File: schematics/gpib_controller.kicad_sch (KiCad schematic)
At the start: 22 parts, among them SW1 SW_DIP_x06, U1 74LS366, U10 74LS04, U12 2716, U2 74LS138

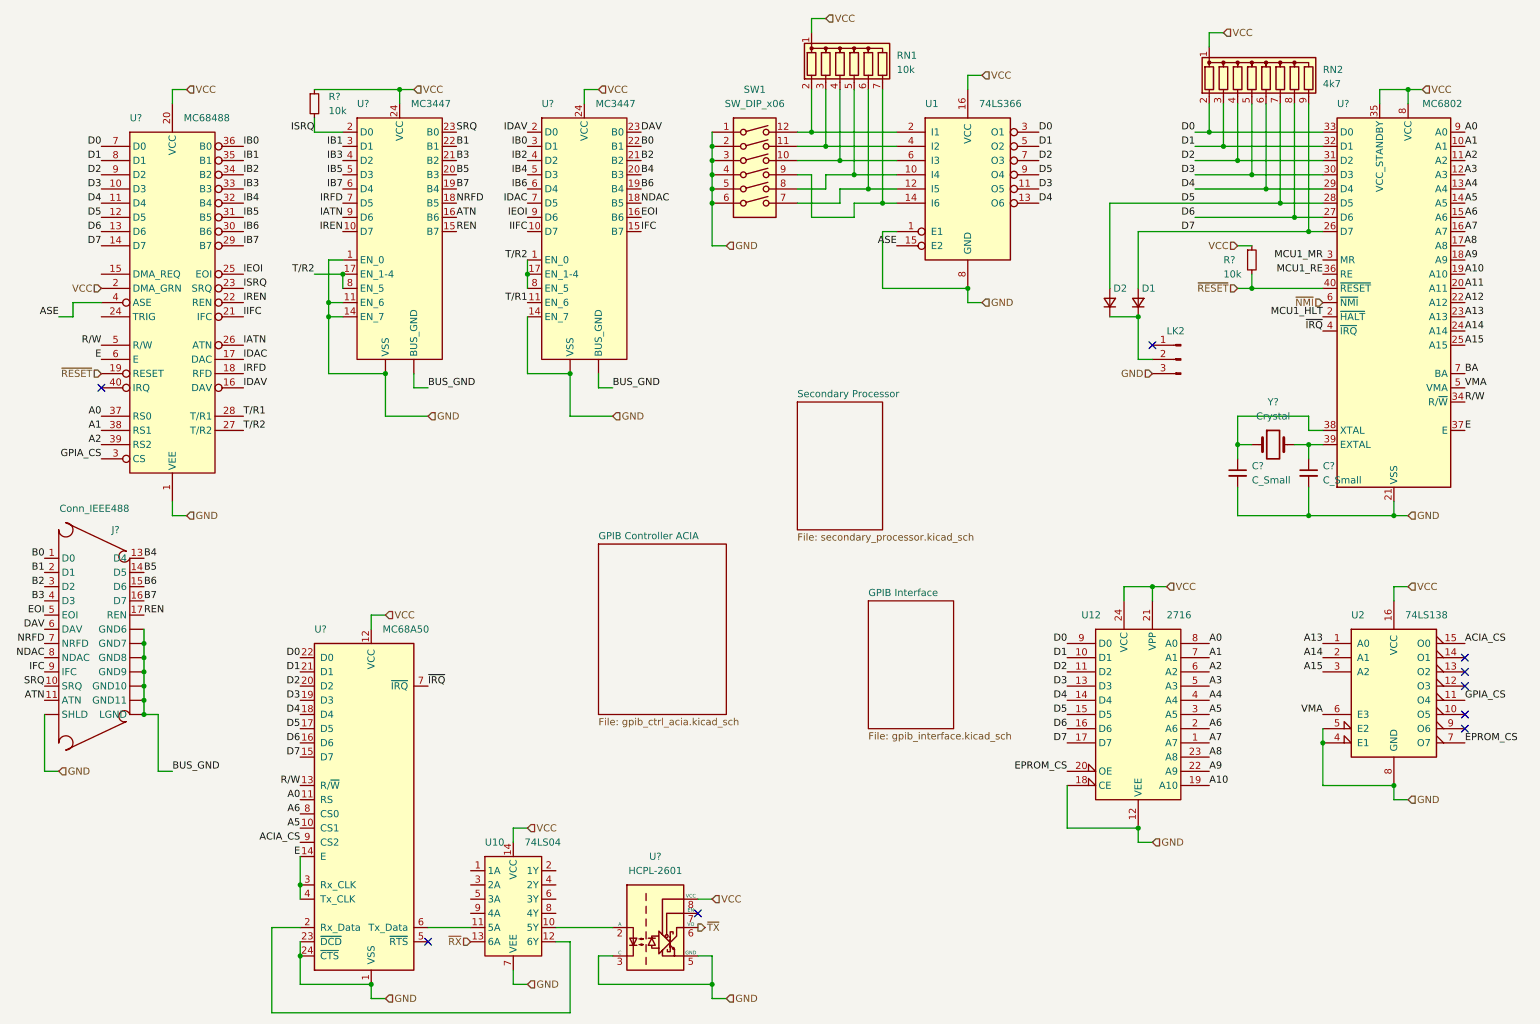
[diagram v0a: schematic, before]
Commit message: Moved more components into hierachical sheets, misc cleanup
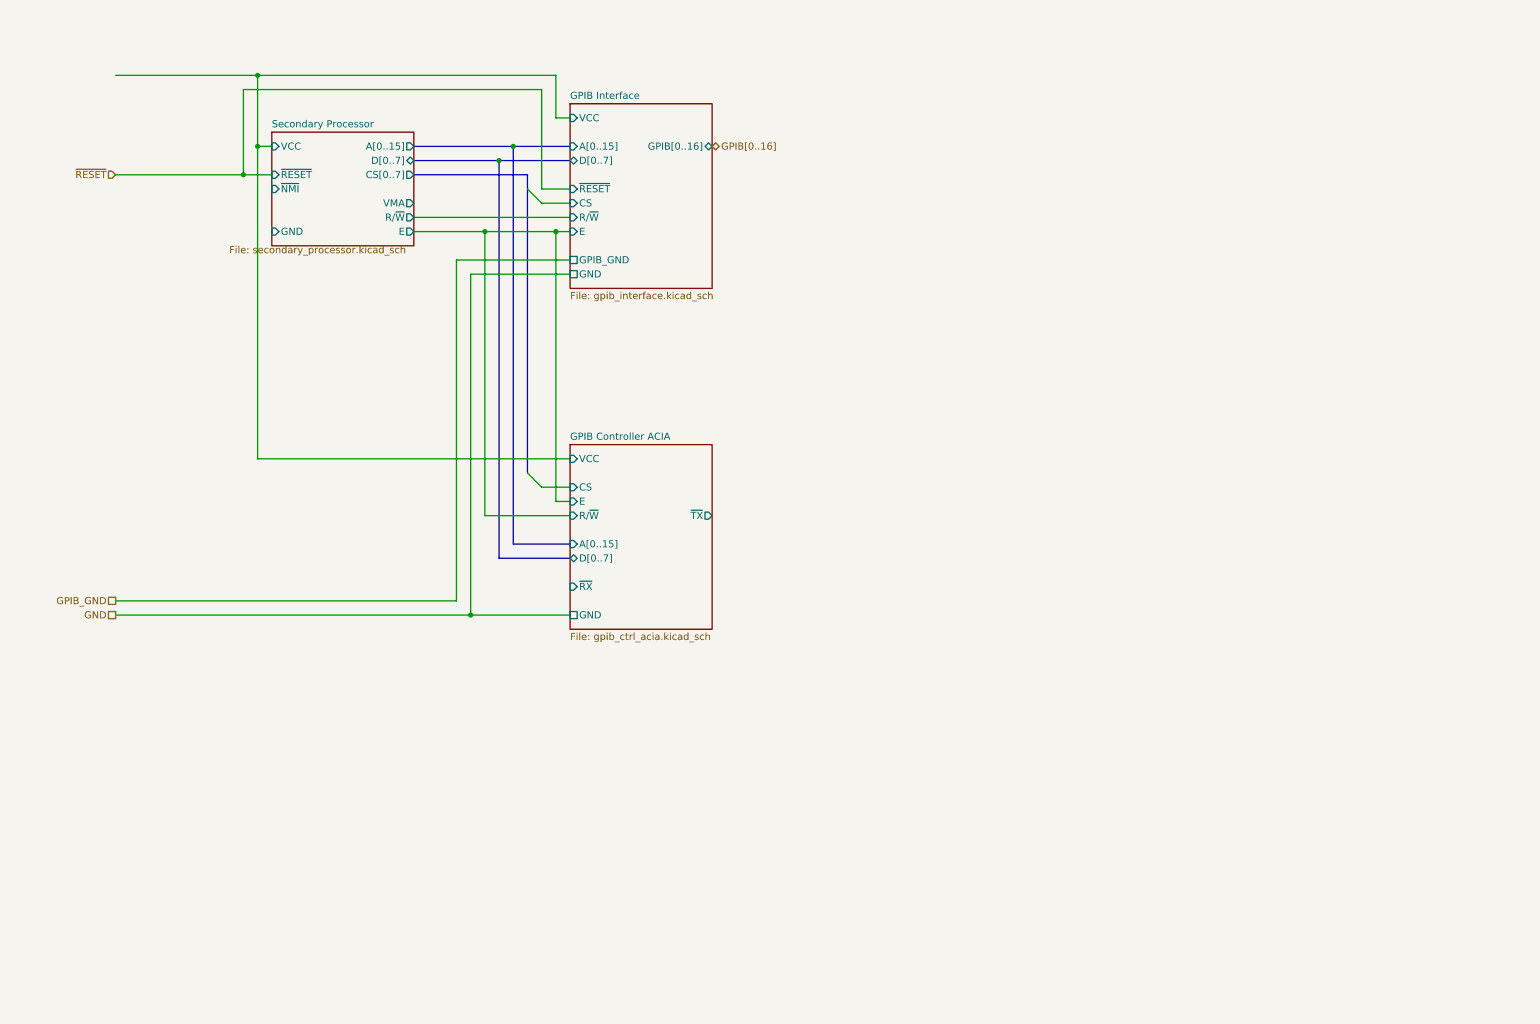
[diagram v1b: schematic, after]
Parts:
- removed C? (x2): C_Small, symbol Device:C_Small
- removed D1, D2: D_Small, symbol Device:D_Small
- removed J?: Conn_IEEE488, symbol Custom:Conn_IEEE488
- removed LK2: Conn_01x03_Male, symbol Connector:Conn_01x03_Male
- removed R? (x2): 10k, symbol Device:R_Small
- removed RN1: 10k, Resistor_THT:R_Array_SIP7, symbol Device:R_Network06
- removed RN2: 4k7, Resistor_THT:R_Array_SIP9, symbol Device:R_Network08
- removed SW1: SW_DIP_x06, symbol Switch:SW_DIP_x06
- removed U1: 74LS366, symbol 74xx:74LS366
- removed U10: 74LS04, symbol Custom:74LS04
- removed U12: 2716, symbol Custom:2716
- removed U2: 74LS138, symbol 74xx:74LS138
- removed U?: MC6802, Package_DIP:DIP-40_W15.24mm, symbol CPU_NXP_6800:MC6802
- removed U?: MC68488, symbol Custom:MC68488
- removed U?: MC68A50, Package_DIP:DIP-40_W15.24mm, symbol Interface_UART:MC68A50
- removed U?: HCPL-2601, Package_DIP:DIP-8_W7.62mm, symbol Isolator:HCPL-2601
- removed U? (x2): MC3447, symbol Custom:MC3447
- removed Y?: Crystal, symbol Device:Crystal
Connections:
- no-connect marks 9 -> 0
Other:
- sheet GPIB Controller ACIA ports: added A[0..15], CS, D[0..7], E, GND, R/~{W}, VCC, ~{RX}, ~{TX}; removed none
- sheet GPIB Interface ports: added A[0..15], CS, D[0..7], E, GND, GPIB[0..16], GPIB_GND, R/~{W}, VCC, ~{RESET}; removed none
- sheet Secondary Processor ports: added A[0..15], CS[0..7], D[0..7], E, GND, R/~{W}, VCC, VMA, ~{NMI}, ~{RESET}; removed none
